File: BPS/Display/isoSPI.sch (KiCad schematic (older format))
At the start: 11 parts, among them J4 isoSPI_Display, U4 LTC6820, U5 HX1188FNL

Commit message: Display, Board Layout
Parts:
- U4: symbol utsvt-bps:LTC6820 -> BPSDisplay-rescue:LTC6820-utsvt-bps
- U5: symbol utsvt-bps:HX1188FNL -> BPSDisplay-rescue:HX1188FNL-utsvt-bps
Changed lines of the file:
@@
 $EndDescr
 $Comp
-L utsvt-bps:LTC6820 U4
+L BPSDisplay-rescue:LTC6820-utsvt-bps U4
 U 1 1 5C4C8CC8
 P 4000 3300
@@
 If the wires lengths are short and you want to save more power, change IBIAS\nresistor to be 2.8k. Look in LTC6820 datasheet for more information on\ncalculating these BIAS resistors.
 $Comp
-L utsvt-bps:HX1188FNL U5
+L BPSDisplay-rescue:HX1188FNL-utsvt-bps U5
 U 1 1 5C4CE5A3
 P 8600 3300
+AR Path="/5C4CE5A3" Ref="U5"  Part="1"
+AR Path="/5D7078DC/5C4CE5A3" Ref="U5"  Part="1"
 F 0 "U5" H 8600 3465 50  0000 C CNN
 F 1 "HX1188FNL" H 8600 3374 50  0000 C CNN

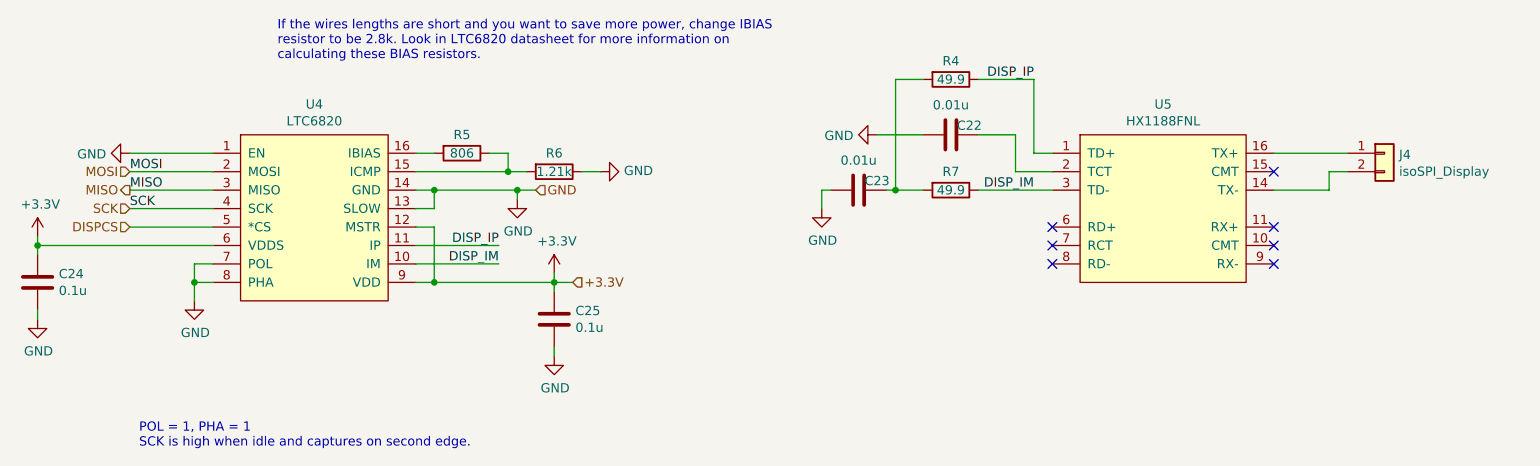
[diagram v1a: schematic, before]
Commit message: Adds display board
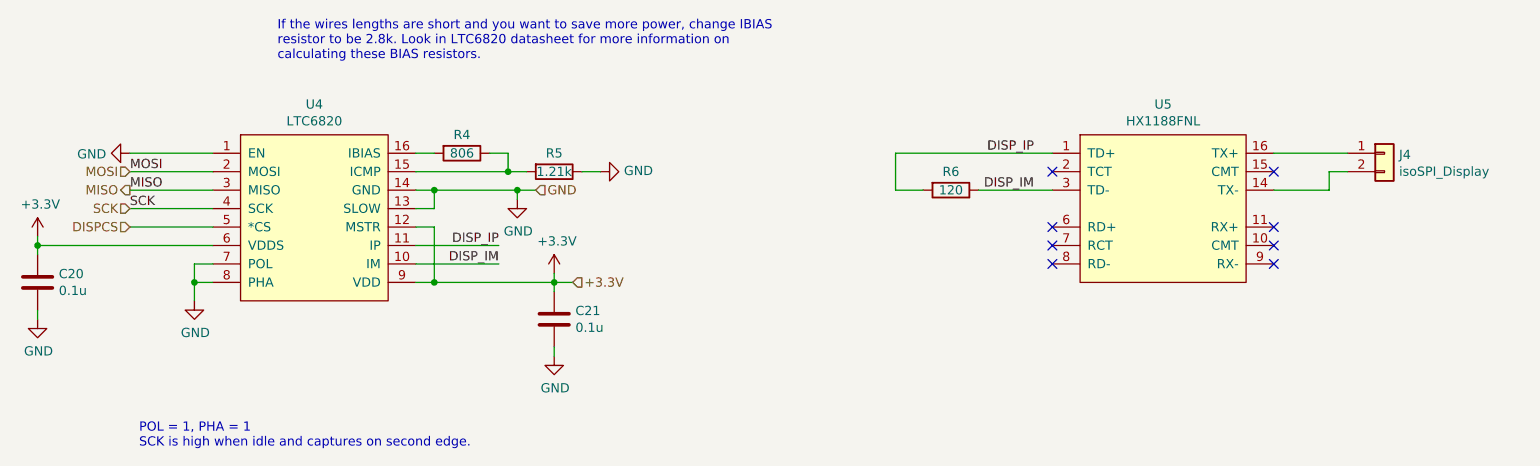
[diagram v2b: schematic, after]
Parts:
- removed C22, C23: 0.01u, Capacitor_SMD:C_0805_2012Metric, symbol Device:C
- removed R4: 49.9, Resistor_SMD:R_0805_2012Metric, symbol Device:R
- R6: renamed from R7; value 49.9 -> 120
- renumbered C24 to C20, C25 to C21, R5 to R4, R6 to R5
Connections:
- net DISP_IP: now also R6.2
- no-connect marks 7 -> 8
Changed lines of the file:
@@
 EESchema Schematic File Version 4
-LIBS:BPSDisplay-cache
-EELAYER 29 0
+EELAYER 30 0
 EELAYER END
 $Descr A4 11693 8268
 encoding utf-8
-Sheet 3 3
+Sheet 3 4
 Title ""
 Date ""
@@
 DISPCS
 $Comp
-L power:GND #PWR0121
+L power:GND #PWR031
 U 1 1 5C4C9040
 P 5100 3650
-F 0 "#PWR0121" H 5100 3400 50  0001 C CNN
+F 0 "#PWR031" H 5100 3400 50  0001 C CNN
 F 1 "GND" H 5105 3477 50  0000 C CNN
 F 2 "" H 5100 3650 50  0001 C CNN
@@
 Connection ~ 5100 3600
 $Comp
-L power:GND #PWR0122
+L power:GND #PWR029
 U 1 1 5C4C933A
 P 3000 3400
-F 0 "#PWR0122" H 3000 3150 50  0001 C CNN
+F 0 "#PWR029" H 3000 3150 50  0001 C CNN
 F 1 "GND" V 3005 3272 50  0000 R CNN
 F 2 "" H 3000 3400 50  0001 C CNN
@@
 $EndComp
 $Comp
-L power:+3.3V #PWR0123
+L power:+3.3V #PWR033
 U 1 1 5C4C945D
 P 5300 4050
-F 0 "#PWR0123" H 5300 3900 50  0001 C CNN
+F 0 "#PWR033" H 5300 3900 50  0001 C CNN
 F 1 "+3.3V" H 5315 4223 50  0000 C CNN
 F 2 "" H 5300 4050 50  0001 C CNN
@@
 Connection ~ 5300 4100
 $Comp
-L power:+3.3V #PWR0124
+L power:+3.3V #PWR032
 U 1 1 5C4C9908
 P 2500 3850
-F 0 "#PWR0124" H 2500 3700 50  0001 C CNN
+F 0 "#PWR032" H 2500 3700 50  0001 C CNN
 F 1 "+3.3V" H 2515 4023 50  0000 C CNN
 F 2 "" H 2500 3850 50  0001 C CNN
@@
 	2500 3900 2500 3850
 $Comp
-L Device:C C24
+L Device:C C20
 U 1 1 5C4C9B05
 P 2500 4100
-F 0 "C24" H 2615 4146 50  0000 L CNN
+F 0 "C20" H 2615 4146 50  0000 L CNN
 F 1 "0.1u" H 2615 4055 50  0000 L CNN
 F 2 "Capacitor_SMD:C_0805_2012Metric" H 2538 3950 50  0001 C CNN
@@
 Connection ~ 2500 3900
 $Comp
-L power:GND #PWR0125
+L power:GND #PWR035
 U 1 1 5C4C9C35
 P 2500 4300
-F 0 "#PWR0125" H 2500 4050 50  0001 C CNN
+F 0 "#PWR035" H 2500 4050 50  0001 C CNN
 F 1 "GND" H 2505 4127 50  0000 C CNN
 F 2 "" H 2500 4300 50  0001 C CNN
@@
 	4650 3600 4550 3600
 $Comp
-L Device:C C25
+L Device:C C21
 U 1 1 5C4CC3A5
 P 5300 4300
-F 0 "C25" H 5415 4346 50  0000 L CNN
+F 0 "C21" H 5415 4346 50  0000 L CNN
 F 1 "0.1u" H 5415 4255 50  0000 L CNN
 F 2 "Capacitor_SMD:C_0805_2012Metric" H 5338 4150 50  0001 C CNN
@@
 $EndComp
 $Comp
-L power:GND #PWR0126
+L power:GND #PWR036
 U 1 1 5C4CC3AC
 P 5300 4500
-F 0 "#PWR0126" H 5300 4250 50  0001 C CNN
+F 0 "#PWR036" H 5300 4250 50  0001 C CNN
 F 1 "GND" H 5305 4327 50  0000 C CNN
 F 2 "" H 5300 4500 50  0001 C CNN
@@
 	5050 3500 4550 3500
 $Comp
-L Device:R R6
+L Device:R R5
 U 1 1 5C4CD755
 P 5300 3500
-F 0 "R6" V 5200 3500 50  0000 C CNN
+F 0 "R5" V 5200 3500 50  0000 C CNN
 F 1 "1.21k" V 5300 3500 50  0000 C CNN
 F 2 "Resistor_SMD:R_0805_2012Metric" V 5230 3500 50  0001 C CNN
@@
 Connection ~ 5050 3500
 $Comp
-L power:GND #PWR0127
+L power:GND #PWR030
 U 1 1 5C4CDCEB
 P 5550 3500
-F 0 "#PWR0127" H 5550 3250 50  0001 C CNN
+F 0 "#PWR030" H 5550 3250 50  0001 C CNN
 F 1 "GND" V 5555 3372 50  0000 R CNN
 F 2 "" H 5550 3500 50  0001 C CNN
@@
 If the wires lengths are short and you want to save more power, change IBIAS\nresistor to be 2.8k. Look in LTC6820 datasheet for more information on\ncalculating these BIAS resistors.
 $Comp
-L BPSDisplay-rescue:HX1188FNL-utsvt-bps U5
+L BPSDisplay-rescue:HX1188FNL-utsvt-bps U?
 U 1 1 5C4CE5A3
 P 8600 3300
-AR Path="/5C4CE5A3" Ref="U5"  Part="1"
+AR Path="/5C4CE5A3" Ref="U?"  Part="1"
 AR Path="/5D7078DC/5C4CE5A3" Ref="U5"  Part="1"
 F 0 "U5" H 8600 3465 50  0000 C CNN
@@
 Wire Wire Line
 	9200 3600 9500 3600
-Wire Wire Line
-	7900 3400 8000 3400
-$Comp
-L Device:R R4
-U 1 1 5C4D2DB3
-P 7450 3000
-F 0 "R4" V 7350 3000 50  0000 C CNN
-F 1 "49.9" V 7450 3000 50  0000 C CNN
-F 2 "Resistor_SMD:R_0805_2012Metric" V 7380 3000 50  0001 C CNN
-F 3 "~" H 7450 3000 50  0001 C CNN
-	1    7450 3000
-	0    1    1    0
-$EndComp
-$Comp
-L Device:R R7
+$Comp
+L Device:R R6
 U 1 1 5C4D2E4C
 P 7450 3600
-F 0 "R7" V 7350 3600 50  0000 C CNN
-F 1 "49.9" V 7450 3600 50  0000 C CNN
+F 0 "R6" V 7350 3600 50  0000 C CNN
+F 1 "120" V 7450 3600 50  0000 C CNN
 F 2 "Resistor_SMD:R_0805_2012Metric" V 7380 3600 50  0001 C CNN
 F 3 "~" H 7450 3600 50  0001 C CNN
@@
 	0    1    1    0
 $EndComp
-$Comp
-L Device:C C23
-U 1 1 5C4D5DB6
-P 6950 3600
-F 0 "C23" V 6900 3700 50  0000 C CNN
-F 1 "0.01u" V 6789 3600 50  0000 C CNN
-F 2 "Capacitor_SMD:C_0805_2012Metric" H 6988 3450 50  0001 C CNN
-F 3 "~" H 6950 3600 50  0001 C CNN
-	1    6950 3600
-	0    1    1    0
-$EndComp
-Wire Wire Line
-	7150 3000 7300 3000
 Wire Wire Line
 	7300 3600 7150 3600
-$Comp
-L power:GND #PWR0128
-U 1 1 5C4D7B1F
-P 6750 3700
-F 0 "#PWR0128" H 6750 3450 50  0001 C CNN
-F 1 "GND" H 6755 3527 50  0000 C CNN
-F 2 "" H 6750 3700 50  0001 C CNN
-F 3 "" H 6750 3700 50  0001 C CNN
-	1    6750 3700
-	1    0    0    -1
-$EndComp
-Wire Wire Line
-	6750 3600 6800 3600
-$Comp
-L Device:C C22
-U 1 1 5C4DFA1E
-P 7450 3300
-F 0 "C22" V 7400 3400 50  0000 C CNN
-F 1 "0.01u" V 7289 3300 50  0000 C CNN
-F 2 "Capacitor_SMD:C_0805_2012Metric" H 7488 3150 50  0001 C CNN
-F 3 "~" H 7450 3300 50  0001 C CNN
-	1    7450 3300
-	0    1    1    0
-$EndComp
-Wire Wire Line
-	7100 3600 7150 3600
-Connection ~ 7150 3600
-Wire Wire Line
-	8000 3500 7800 3500
-Wire Wire Line
-	7800 3500 7800 3300
-Wire Wire Line
-	7800 3300 7600 3300
-Wire Wire Line
-	7150 3000 7150 3600
-Wire Wire Line
-	7900 3000 7900 3400
-$Comp
-L power:GND #PWR0129
-U 1 1 5C4EA1BB
-P 7050 3300
-F 0 "#PWR0129" H 7050 3050 50  0001 C CNN
-F 1 "GND" V 7055 3172 50  0000 R CNN
-F 2 "" H 7050 3300 50  0001 C CNN
-F 3 "" H 7050 3300 50  0001 C CNN
-	1    7050 3300
-	0    1    1    0
-$EndComp
 Text Label 3000 3500 0    50   ~ 0
 MOSI
@@
 SCK
 Wire Wire Line
-	7600 3000 7900 3000
-Wire Wire Line
 	7600 3600 8000 3600
-Wire Wire Line
-	6750 3700 6750 3600
-Wire Wire Line
-	7050 3300 7300 3300
-Text Label 7900 3000 2    50   ~ 0
+Text Label 7900 3400 2    50   ~ 0
 DISP_IP
 Text Label 7900 3600 2    50   ~ 0
@@
 DISP_IM
 $Comp
-L Device:R R5
+L Device:R R4
 U 1 1 5C4CCDCF
 P 4800 3400
-F 0 "R5" V 4700 3400 50  0000 C CNN
+F 0 "R4" V 4700 3400 50  0000 C CNN
 F 1 "806" V 4800 3400 50  0000 C CNN
 F 2 "Resistor_SMD:R_0805_2012Metric" V 4730 3400 50  0001 C CNN
@@
 	2500 3900 3450 3900
 $Comp
-L power:GND #PWR0130
+L power:GND #PWR034
 U 1 1 5D6DBB55
 P 3350 4200
-F 0 "#PWR0130" H 3350 3950 50  0001 C CNN
+F 0 "#PWR034" H 3350 3950 50  0001 C CNN
 F 1 "GND" H 3355 4027 50  0000 C CNN
 F 2 "" H 3350 4200 50  0001 C CNN
@@
 Wire Wire Line
 	3350 4100 3350 4200
+NoConn ~ 8000 3500
+Wire Wire Line
+	7150 3400 7150 3600
+Wire Wire Line
+	7150 3400 8000 3400
 $EndSCHEMATC
